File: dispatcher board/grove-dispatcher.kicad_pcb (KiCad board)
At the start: 2 copper layers, 156.8 x 75.6 mm, 53 parts, among them P1 CONN_01X12, P10 CONN_01X06, P11 CONN_01X06, P12 CONN_01X06, P13 CONN_01X06, P14 CONN_01X06, P15 CONN_01X06, P16 CONN_01X06, P17 CONN_01X06, P2 CONN_01X06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

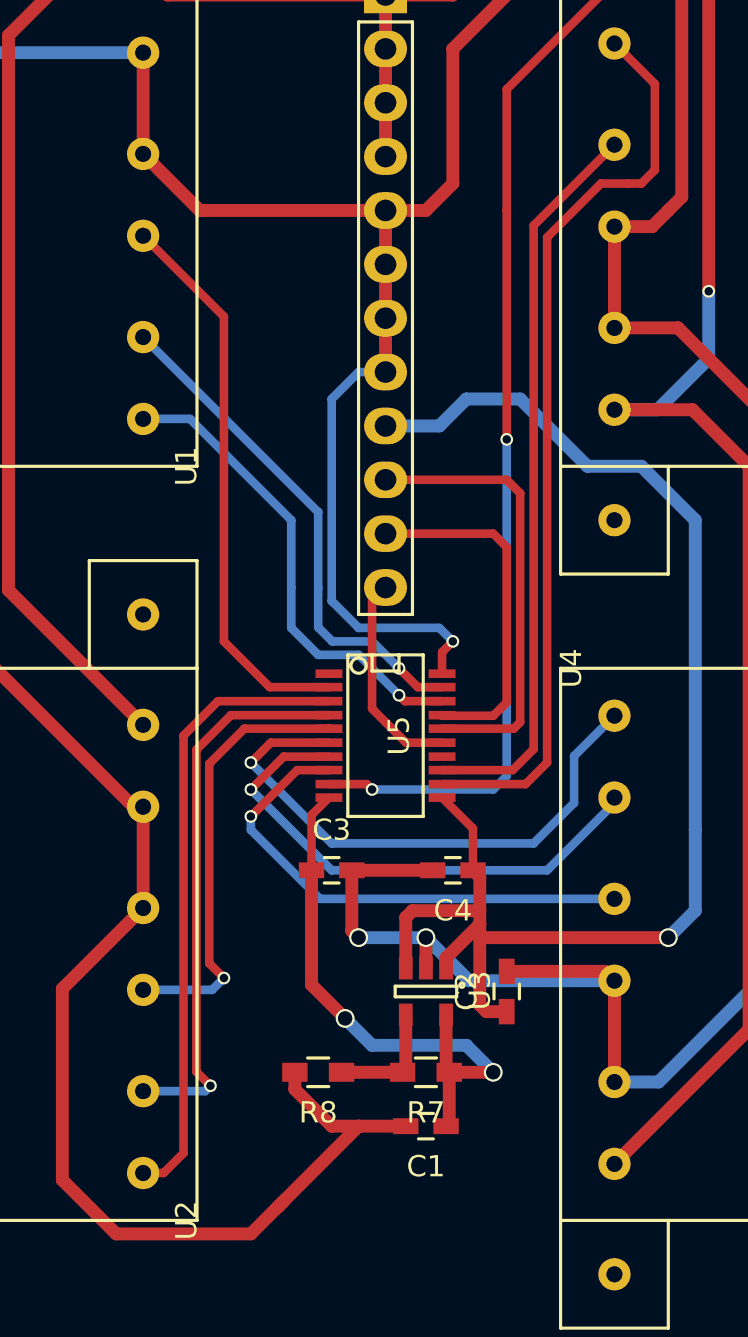
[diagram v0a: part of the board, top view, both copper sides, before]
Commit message: Add some test points
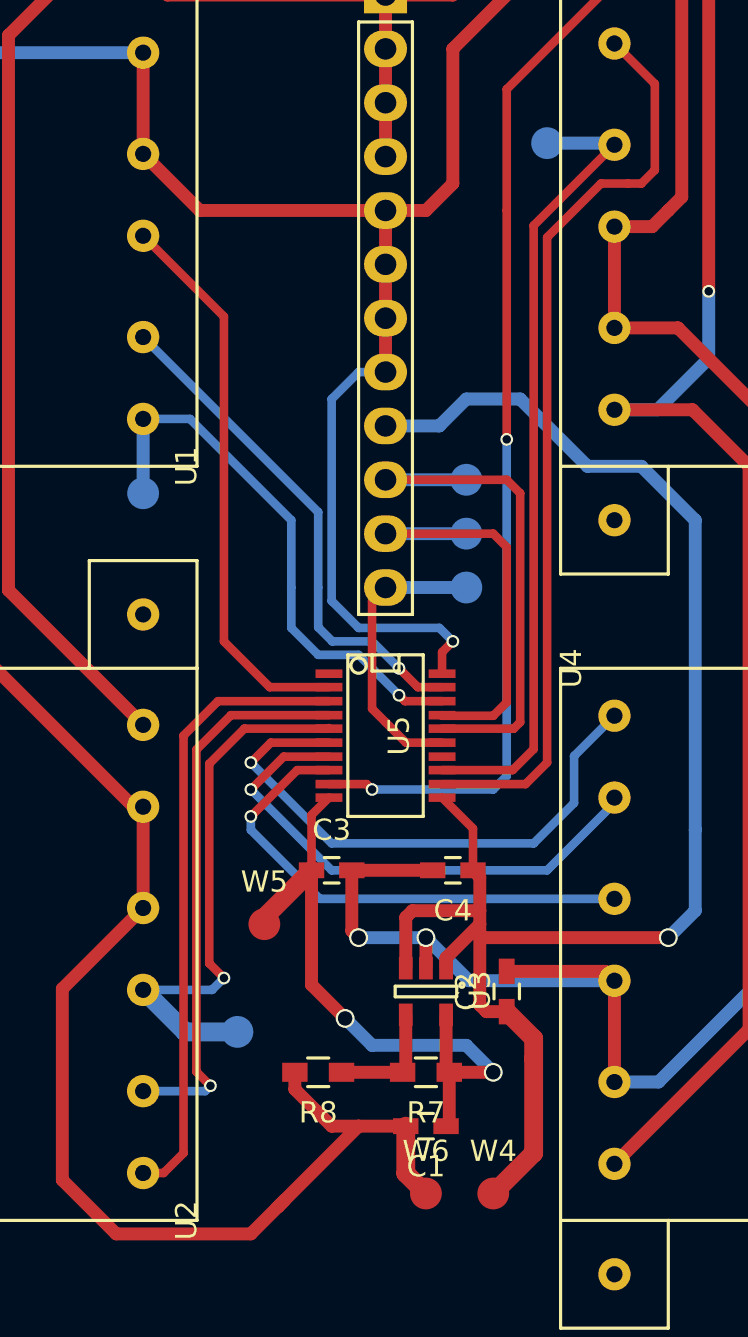
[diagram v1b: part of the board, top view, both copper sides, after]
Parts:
- added W1: SCLK, Measurement_Points:Measurement_Point_Round-SMD-Pad_Small, B.Cu at (144.1, 91.4)
- added W2: MOSI, Measurement_Points:Measurement_Point_Round-SMD-Pad_Small, B.Cu at (144.1, 94.0)
- added W3: CS, Measurement_Points:Measurement_Point_Round-SMD-Pad_Small, B.Cu at (144.1, 96.5)
- added W4: 5V, Measurement_Points:Measurement_Point_Round-SMD-Pad_Small, F.Cu at (145.4, 125.1)
- added W5: 2V5, Measurement_Points:Measurement_Point_Round-SMD-Pad_Small, F.Cu at (134.6, 112.4)
- added W6: GND, Measurement_Points:Measurement_Point_Round-SMD-Pad_Small, F.Cu at (142.2, 125.1)
- added W7: AO1, Measurement_Points:Measurement_Point_Round-SMD-Pad_Small, B.Cu at (128.9, 92.1)
- added W8: AO6, Measurement_Points:Measurement_Point_Round-SMD-Pad_Small, B.Cu at (133.3, 117.5)
- added W9: AO12, Measurement_Points:Measurement_Point_Round-SMD-Pad_Small, B.Cu at (148.0, 75.6)
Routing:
- net +5V: track 67.3 -> 77.2 mm
- net /AO6: track 20.8 -> 26.1 mm
- net /SCLK_5V: track 21.2 -> 25.0 mm
- net /MOSI_5V: track 16.6 -> 20.4 mm
- net /CS_5V: track 9.94 -> 13.8 mm
- net GND: track 263.6 -> 267.2 mm
- net /AO1: track 22.6 -> 26.1 mm
- net +2V5: track 26.9 -> 30.4 mm
- net /AO12: track 34.8 -> 38.0 mm

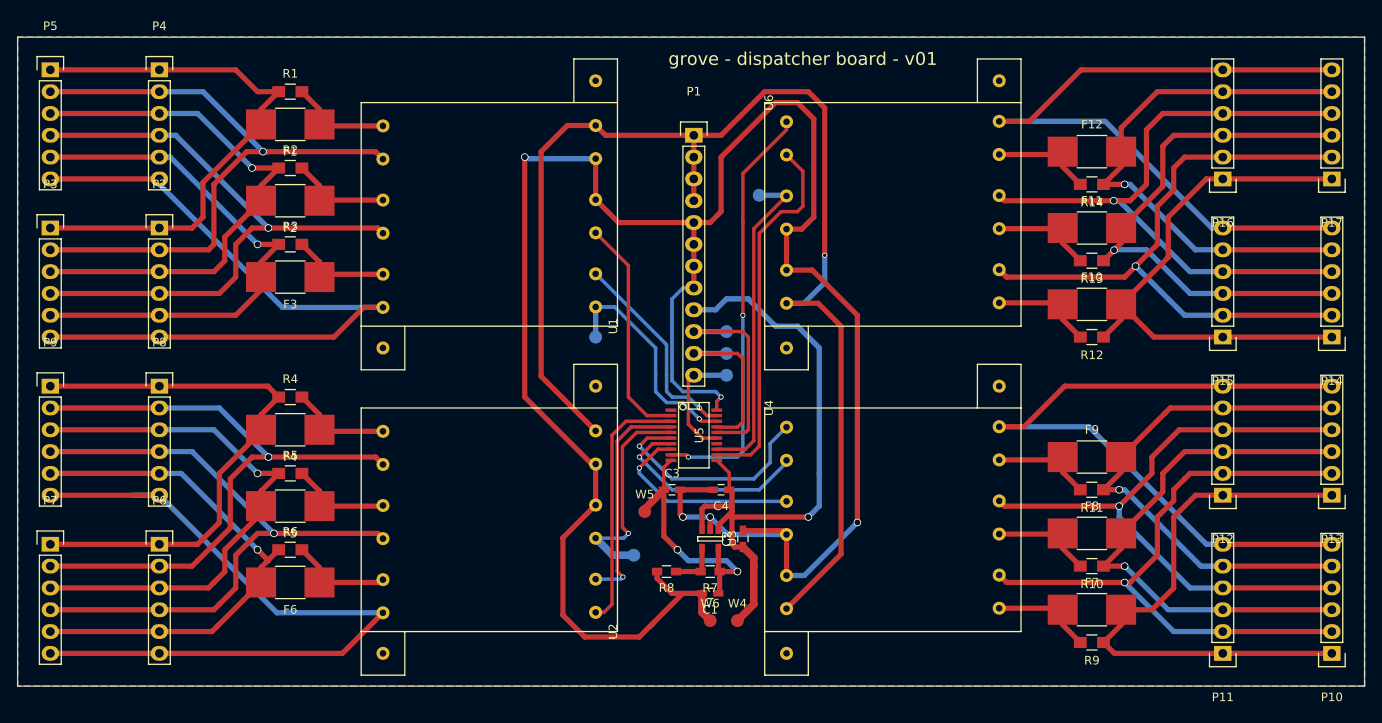
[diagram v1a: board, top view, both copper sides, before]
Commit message: Added mouting holes
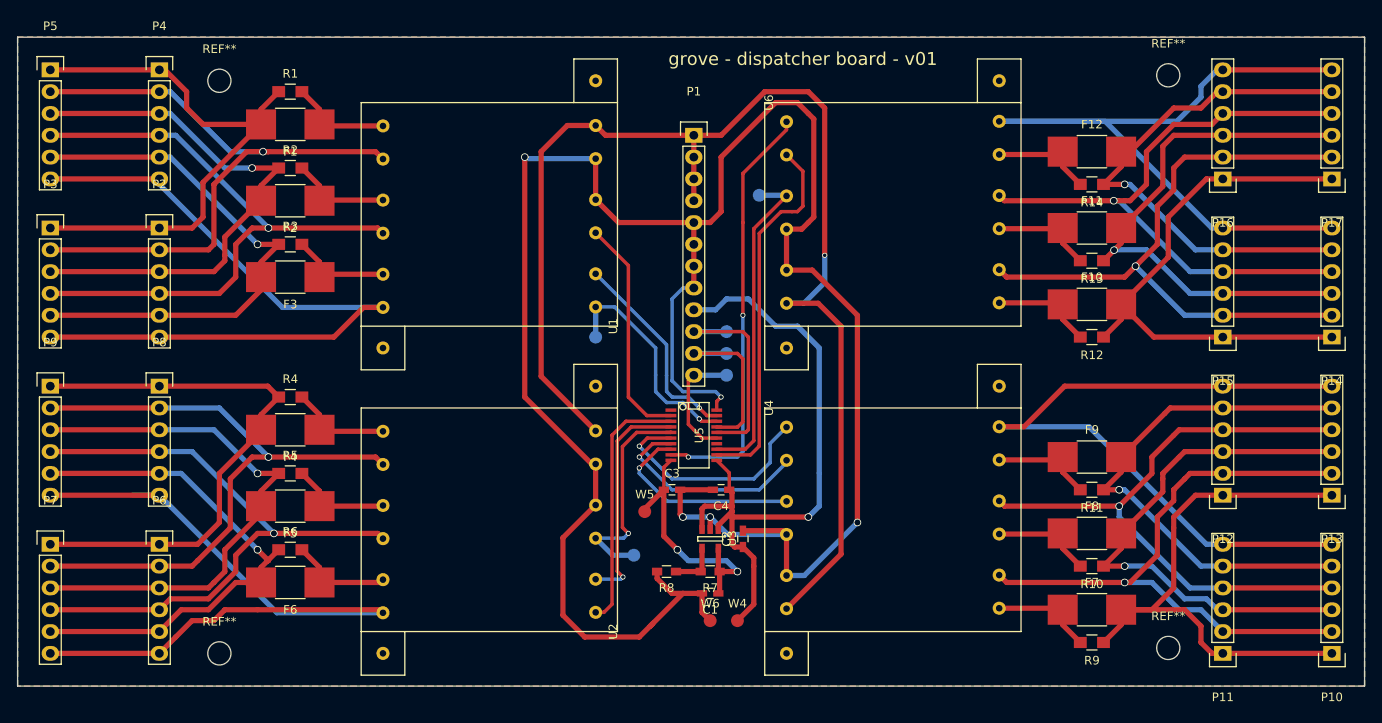
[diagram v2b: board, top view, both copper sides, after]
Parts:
- added REF**: MountingHole_2.7mm, Mounting_Holes:MountingHole_2.7mm, F.Cu at (85.1, 62.2)
- added REF**: MountingHole_2.7mm, Mounting_Holes:MountingHole_2.7mm, F.Cu at (195.6, 128.3)
- added REF**: MountingHole_2.7mm, Mounting_Holes:MountingHole_2.7mm, F.Cu at (195.6, 61.6)
- added REF**: MountingHole_2.7mm, Mounting_Holes:MountingHole_2.7mm, F.Cu at (85.1, 128.9)
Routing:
- net Net-(F12-Pad2): track 63.5 -> 61.8 mm
- net Net-(P14-Pad4): track 75.7 -> 74.2 mm
- net Net-(P6-Pad4): track 74.9 -> 73.8 mm
- net Net-(P14-Pad6): track 85.1 -> 85.8 mm
- net Net-(F7-Pad2): track 66.7 -> 67.3 mm
- net Net-(F1-Pad2): track 64.6 -> 65.2 mm

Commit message: Add layout for resistors + more test points
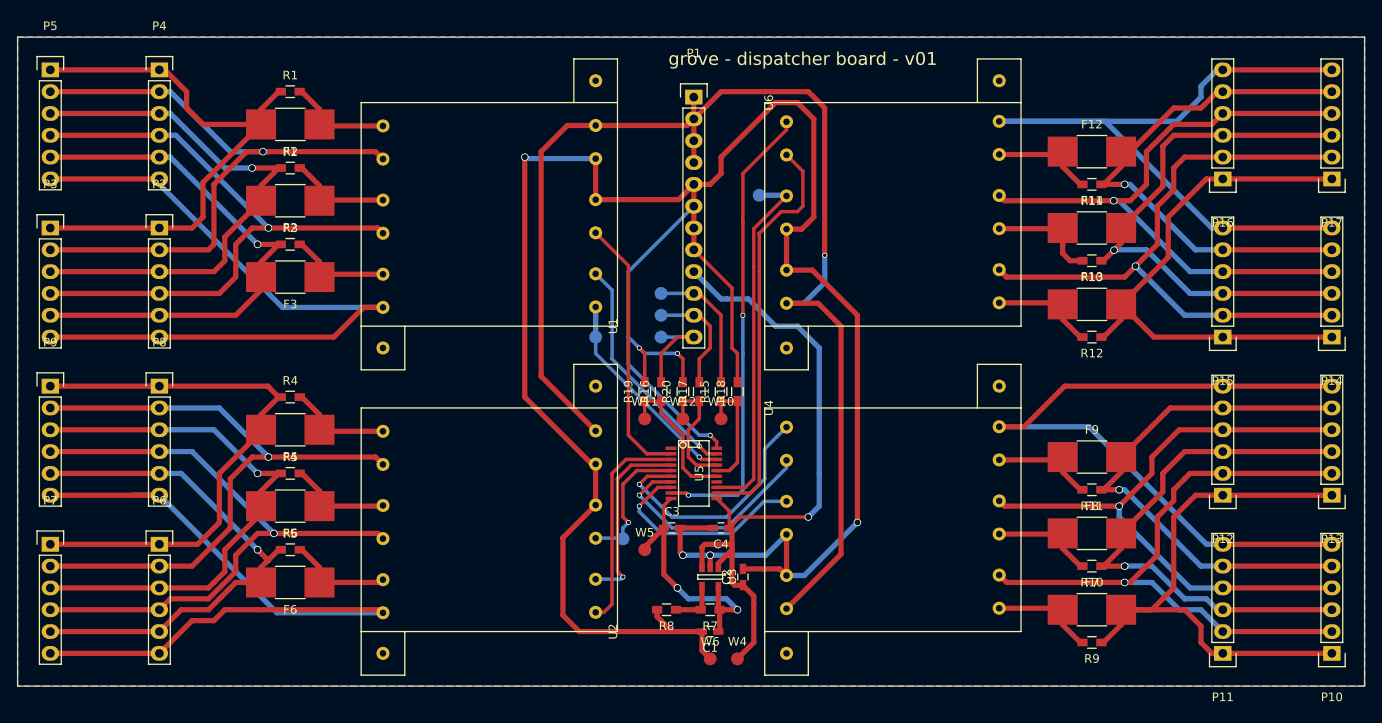
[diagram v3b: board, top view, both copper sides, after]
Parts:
- removed REF** (x4): MountingHole_2.7mm, Mounting_Holes:MountingHole_2.7mm
- added R15: 10ohm, Resistors_SMD:R_0603_HandSoldering, F.Cu at (143.5, 98.4)
- added R16: 10ohm, Resistors_SMD:R_0603_HandSoldering, F.Cu at (136.5, 98.4)
- added R17: 10ohm, Resistors_SMD:R_0603_HandSoldering, F.Cu at (141.0, 98.4)
- added R18: 1kOhm, Resistors_SMD:R_0603_HandSoldering, F.Cu at (145.4, 98.4)
- added R19: 1kOhm, Resistors_SMD:R_0603_HandSoldering, F.Cu at (134.6, 98.4)
- added R20: 1kOhm, Resistors_SMD:R_0603_HandSoldering, F.Cu at (139.1, 98.4)
- added W10: SCLK_F, Measurement_Points:Measurement_Point_Round-SMD-Pad_Small, F.Cu at (143.5, 101.6)
- added W11: CS_F, Measurement_Points:Measurement_Point_Round-SMD-Pad_Small, F.Cu at (134.6, 101.6)
- added W12: MOSI_F, Measurement_Points:Measurement_Point_Round-SMD-Pad_Small, F.Cu at (139.1, 101.6)
- R1, R10, R11, R12, R13, R14, R2, R3, R4, R5, R6, R9: footprint Resistors_SMD:R_0805_HandSoldering -> Resistors_SMD:R_0603_HandSoldering
- moved W2 8.82 mm to (136.5, 89.5)
- moved W1 8.82 mm to (136.5, 87.0)
- moved W3 8.82 mm to (136.5, 92.1)
- moved C2 4.45 mm to (146.1, 120.0)
- moved R7 4.45 mm to (142.2, 123.8)
- moved R8 4.45 mm to (137.2, 123.8)
- moved U3 4.45 mm to (142.2, 120.0)
- moved U5 4.45 mm to (140.3, 108.0)
- moved W5 4.45 mm to (134.6, 116.8)
- moved C1 4.44 mm to (142.2, 126.4)
- moved C3 4.44 mm to (137.8, 114.3)
- moved C4 4.44 mm to (143.5, 114.3)
- moved P1 4.44 mm to (140.3, 64.1)
- moved W4 4.44 mm to (145.4, 129.5)
- moved W6 4.44 mm to (142.2, 129.5)
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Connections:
- U5 pad 15: /CS_5V -> Net-(R16-Pad1)
- U5 pad 16: /SCLK_5V -> Net-(R15-Pad1)
- U5 pad 17: /MOSI_5V -> Net-(R17-Pad1)
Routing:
- net GND: track 267.2 -> 306.0 mm, vias 5 -> 7
- net Net-(R16-Pad1): track 0.00 -> 17.2 mm
- net Net-(R17-Pad1): track 0.00 -> 14.7 mm
- net Net-(R15-Pad1): track 0.00 -> 13.9 mm
- net /AO6: track 26.1 -> 16.4 mm
- net /SCLK_5V: track 25.0 -> 15.8 mm
- net /MOSI_5V: track 20.4 -> 13.3 mm
- net /AO11: track 43.3 -> 47.9 mm
- net /AO3: track 26.6 -> 31.1 mm
- net /AO4: track 29.5 -> 25.1 mm
- net /AO12: track 38.0 -> 42.5 mm
- net /AO10: track 49.3 -> 53.7 mm
- net /AO5: track 26.3 -> 21.9 mm
- net /AO2: track 24.1 -> 27.5 mm
- net /AO7: track 26.6 -> 29.2 mm
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
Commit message: Update the pico buck footprint to fix pin placement error
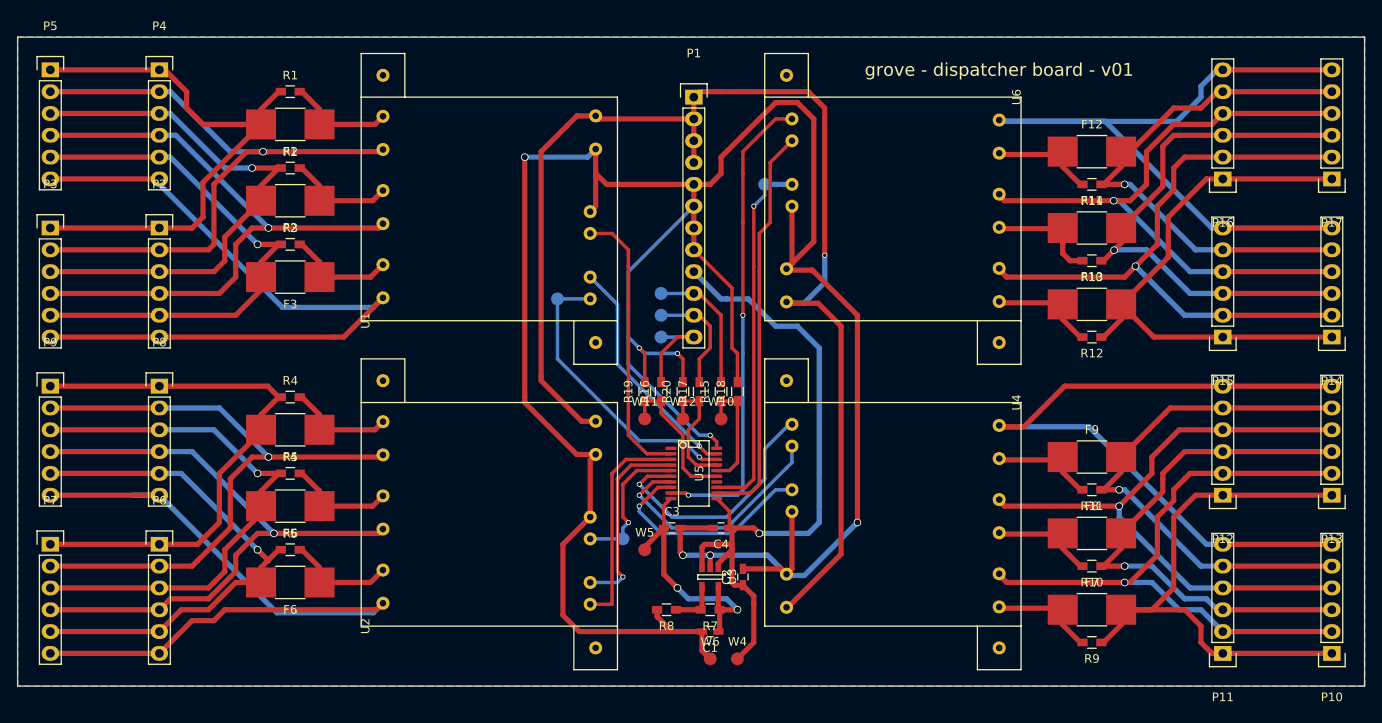
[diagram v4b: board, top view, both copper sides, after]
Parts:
- moved U1 29.9 mm to (101.6, 64.1)
- moved U2 29.9 mm to (101.6, 99.7)
- moved U4 29.9 mm to (178.4, 125.7)
- moved U6 29.9 mm to (178.4, 90.2)
- moved W7 6.29 mm to (124.5, 87.6)
- moved W9 1.42 mm to (148.6, 74.3)
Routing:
- net GND: track 306.0 -> 318.7 mm
- net /AO1: track 24.6 -> 34.2 mm
- net /AO3: track 31.1 -> 32.8 mm
- net /AO10: track 53.7 -> 55.4 mm
- net /AO8: track 27.1 -> 28.7 mm
- net +5V: track 78.8 -> 80.4 mm
- net /AO9: track 25.0 -> 26.2 mm
- net Net-(F3-Pad1): track 12.2 -> 13.1 mm
- net Net-(P2-Pad6): track 85.5 -> 86.4 mm
- net /V+: track 148.2 -> 147.3 mm
- net /AO11: track 47.9 -> 47.0 mm
- net /AO5: track 21.9 -> 22.7 mm
- net /AO6: track 16.4 -> 17.1 mm
- net Net-(P6-Pad6): track 88.6 -> 89.2 mm
- net Net-(F2-Pad1): track 12.1 -> 12.7 mm
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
